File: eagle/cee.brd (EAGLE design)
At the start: 50 x 80 mm, 55 parts, among them IC1 IC1, J1 SOLDERJUMPERNC2

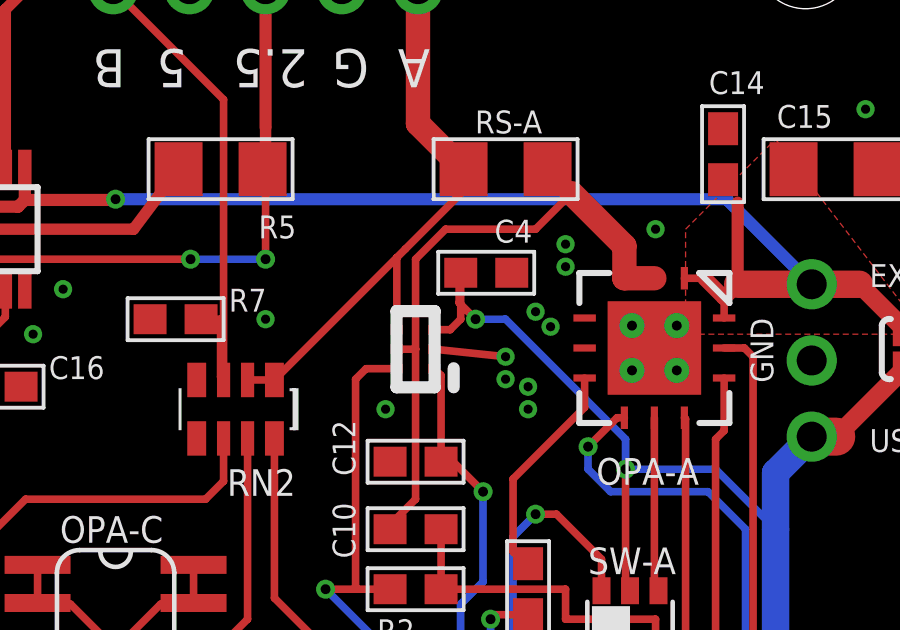
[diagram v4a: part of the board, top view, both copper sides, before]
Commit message: Update library (SC70 and QFN)
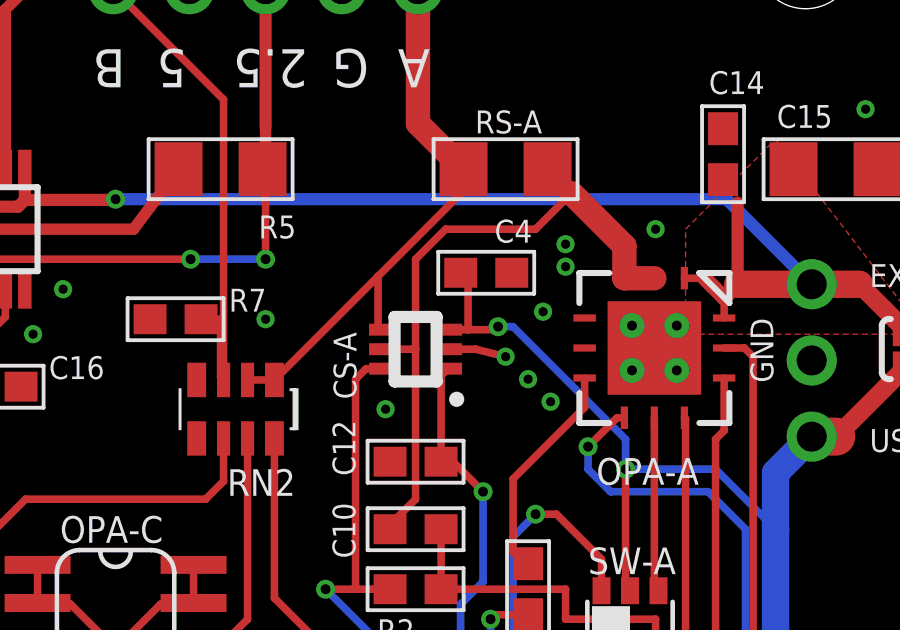
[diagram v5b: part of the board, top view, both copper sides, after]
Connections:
- net GND: now also OPA-A.P$2, OPA-A.P$4, OPA-A.P$6, OPA-A.P$7
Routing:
- net 5V: track 185.1 -> 183.6 mm
- net SMU-A: track 19.6 -> 19.0 mm
- net GND: track 22.6 -> 22.2 mm, vias 48 -> 46
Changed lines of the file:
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@@
 <wire x1="46.542" y1="59.6051" x2="44.0219" y2="57.085" width="0.6096" layer="1"/>
 <wire x1="44.0219" y1="57.085" x2="43.2052" y2="57.085" width="1.27" layer="1"/>
-<wire x1="30.625" y1="60.65" x2="31.155" y2="60.65" width="0.254" layer="1"/>
-<wire x1="31.155" y1="60.65" x2="31.505" y2="61" width="0.254" layer="1"/>
+<wire x1="31.1" y1="60.65" x2="31.155" y2="60.65" width="0.254" layer="1"/>
 <wire x1="42" y1="14" x2="42" y2="54" width="0.9144" layer="16"/>
 <wire x1="42" y1="54" x2="42" y2="55.8798" width="0.9144" layer="16"/>
@@
 <wire x1="13.85" y1="49.25" x2="14" y2="49.1" width="0.254" layer="1"/>
 <wire x1="14" y1="49.1" x2="14" y2="49" width="0.254" layer="1"/>
-<wire x1="31.505" y1="61" x2="31.505" y2="62.548" width="0.254" layer="1"/>
 <wire x1="31.505" y1="62.548" x2="31.452" y2="62.548" width="0.254" layer="1"/>
-<wire x1="31.452" y1="62.548" x2="31.452" y2="61.548" width="0.254" layer="1"/>
-<wire x1="31.452" y1="61.548" x2="32" y2="61" width="0.254" layer="1"/>
-<via x="32" y="61" extent="1-16" drill="0.3302"/>
-<wire x1="32" y1="61" x2="33" y2="61" width="0.254" layer="16"/>
-<wire x1="33" y1="61" x2="37" y2="57" width="0.254" layer="16"/>
+<via x="32.75" y="60.75" extent="1-16" drill="0.3302"/>
+<wire x1="32.75" y1="60.75" x2="33.25" y2="60.75" width="0.254" layer="16"/>
+<wire x1="33.25" y1="60.75" x2="37" y2="57" width="0.254" layer="16"/>
 <wire x1="37" y1="57" x2="37" y2="56" width="0.254" layer="16"/>
 <via x="37" y="56" extent="1-16" drill="0.3302"/>
@@
 <wire x1="37" y1="56" x2="40" y2="56" width="0.254" layer="16"/>
 <wire x1="40" y1="56" x2="42" y2="54" width="0.254" layer="16"/>
+<wire x1="32.75" y1="60.75" x2="32.65" y2="60.65" width="0.254" layer="1"/>
+<wire x1="32.65" y1="60.65" x2="31.75" y2="60.65" width="0.254" layer="1"/>
+<wire x1="31.75" y1="60.65" x2="31.1" y2="60.65" width="0.254" layer="1"/>
+<wire x1="31.505" y1="62.548" x2="31.75" y2="62.303" width="0.254" layer="1"/>
+<wire x1="31.75" y1="62.303" x2="31.75" y2="60.65" width="0.254" layer="1"/>
 </signal>
 <signal name="GND">
@@
 <via x="20" y="32" extent="1-16" drill="0.305"/>
 <via x="21.25" y="21.5" extent="1-16" drill="0.305"/>
-<via x="33.75" y="58" extent="1-16" drill="0.305"/>
 <via x="36" y="48" extent="1-16" drill="0.305"/>
 <via x="25" y="50" extent="1-16" drill="0.305"/>
@@
 <via x="35" y="62.75" extent="1-16" drill="0.305"/>
 <via x="33" y="59.75" extent="1-16" drill="0.305"/>
-<wire x1="30.625" y1="60" x2="33" y2="59.75" width="0.254" layer="1"/>
+<wire x1="31.1" y1="60" x2="32" y2="60" width="0.254" layer="1"/>
+<wire x1="32" y1="60" x2="33" y2="59.75" width="0.254" layer="1"/>
 <contactref element="C16" pad="2"/>
 <via x="30.5" y="30.25" extent="1-16" drill="0.3302" shape="octagon"/>
@@
 <contactref element="C17" pad="1"/>
 <via x="29" y="58" extent="1-16" drill="0.305"/>
-<via x="33" y="59" extent="1-16" drill="0.305"/>
-<via x="33.75" y="58.75" extent="1-16" drill="0.305"/>
+<via x="33.75" y="59" extent="1-16" drill="0.305"/>
+<via x="34.5" y="58.25" extent="1-16" drill="0.305"/>
 <via x="17" y="43.5" extent="1-16" drill="0.305"/>
 <via x="31.25" y="36.25" extent="1-16" drill="0.3302" shape="octagon"/>
@@
 <via x="34.25" y="38.25" extent="1-16" drill="0.3302" shape="octagon"/>
 <via x="27.75" y="45.25" extent="1-16" drill="0.3302" shape="octagon"/>
-<via x="34" y="61.25" extent="1-16" drill="0.305"/>
-<via x="34.5" y="60.75" extent="1-16" drill="0.305"/>
+<via x="34.25" y="61.25" extent="1-16" drill="0.305"/>
 <via x="5" y="43" extent="1-16" drill="0.305"/>
 <via x="17.25" y="60.5" extent="1-16" drill="0.305"/>
@@
 <via x="18.25" y="62" extent="1-16" drill="0.305"/>
 <wire x1="20" y1="30" x2="20.5" y2="29.5" width="0.254" layer="1"/>
+<contactref element="OPA-A" pad="P$2"/>
+<contactref element="OPA-A" pad="P$4"/>
+<contactref element="OPA-A" pad="P$6"/>
+<contactref element="OPA-A" pad="P$7"/>
 </signal>
 <signal name="PDI-DATA">
@@
 <wire x1="25.295" y1="58.975" x2="24.4" y2="58.975" width="0.254" layer="1"/>
 <wire x1="31.6" y1="66" x2="31.6" y2="65.28" width="0.254" layer="1"/>
-<wire x1="31.6" y1="65.28" x2="29.66" y2="63.34" width="0.254" layer="1"/>
-<wire x1="29.375" y1="63.055" x2="25.295" y2="58.975" width="0.254" layer="1"/>
-<wire x1="29.375" y1="60.65" x2="29.375" y2="63.055" width="0.254" layer="1"/>
-<wire x1="29.375" y1="63.055" x2="29.66" y2="63.34" width="0.254" layer="1"/>
+<wire x1="31.6" y1="65.28" x2="28.75" y2="62.43" width="0.254" layer="1"/>
+<wire x1="28.75" y1="62.43" x2="25.295" y2="58.975" width="0.254" layer="1"/>
+<wire x1="28.75" y1="62.43" x2="28.75" y2="60.75" width="0.254" layer="1"/>
+<wire x1="28.75" y1="60.75" x2="28.85" y2="60.65" width="0.254" layer="1"/>
+<wire x1="28.85" y1="60.65" x2="28.9" y2="60.65" width="0.254" layer="1"/>
 </signal>
 <signal name="EXP3">
@@
 <wire x1="36.96" y1="62.365" x2="37.96" y2="62.365" width="0.8128" layer="1"/>
 <wire x1="34" y1="64" x2="35.2" y2="65.2" width="0.254" layer="1"/>
-<wire x1="29.375" y1="60" x2="30" y2="60" width="0.254" layer="1"/>
+<wire x1="28.9" y1="60" x2="30" y2="60" width="0.254" layer="1"/>
 <wire x1="34" y1="64" x2="31" y2="64" width="0.254" layer="1"/>
 <wire x1="30" y1="60" x2="30" y2="63" width="0.254" layer="1"/>
@@
 <wire x1="32.6" y1="26.6" x2="33.25" y2="27.25" width="0.254" layer="1"/>
 <contactref element="CS-A" pad="P6"/>
-<wire x1="29.375" y1="59.35" x2="28.35" y2="59.35" width="0.254" layer="1"/>
+<wire x1="28.9" y1="59.35" x2="28.35" y2="59.35" width="0.254" layer="1"/>
 <wire x1="28.35" y1="59.35" x2="28" y2="59" width="0.254" layer="1"/>
 <wire x1="28" y1="59" x2="28" y2="52" width="0.254" layer="1"/>
@@
 <contactref element="C12" pad="1"/>
 <wire x1="30.85" y1="56.25" x2="30.85" y2="59.125" width="0.254" layer="1"/>
-<wire x1="30.85" y1="59.125" x2="30.625" y2="59.35" width="0.254" layer="1"/>
+<wire x1="30.85" y1="59.125" x2="31.1" y2="59.35" width="0.254" layer="1"/>
 <wire x1="30.85" y1="56.25" x2="31.25" y2="56.25" width="0.254" layer="1"/>
 <wire x1="31.25" y1="56.25" x2="32.25" y2="55.25" width="0.254" layer="1"/>

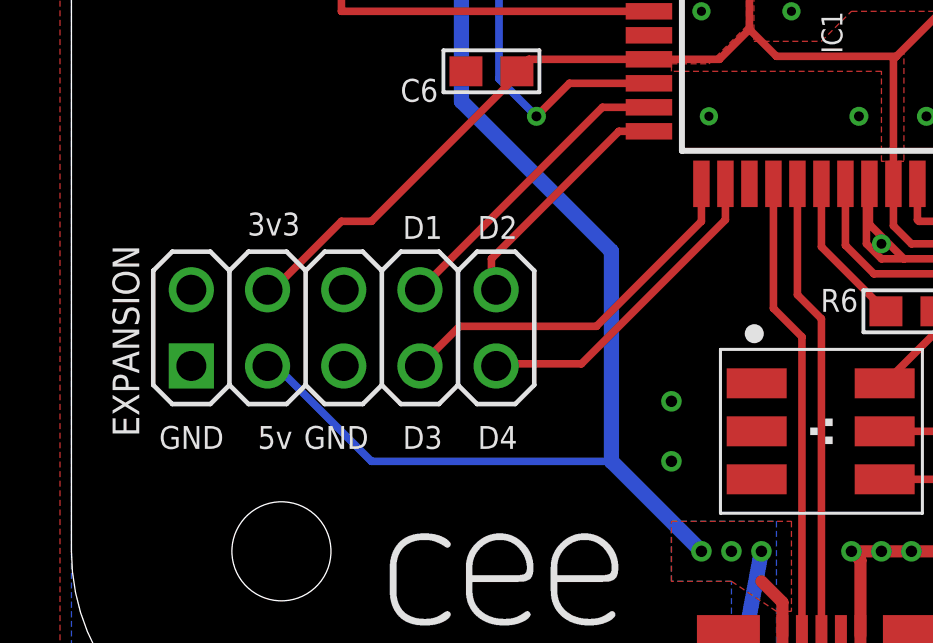
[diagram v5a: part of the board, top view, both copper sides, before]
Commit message: Break out another GPIO
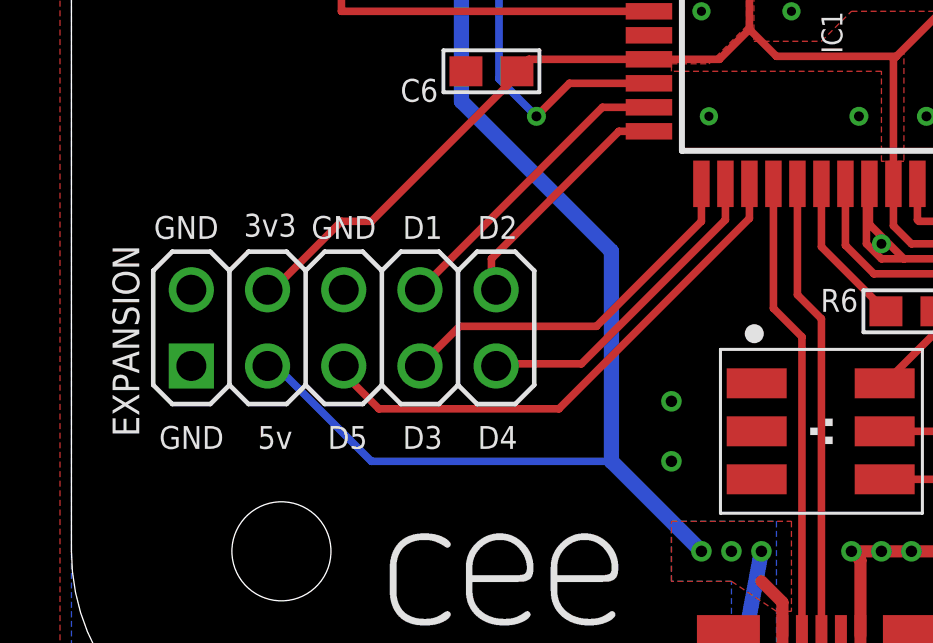
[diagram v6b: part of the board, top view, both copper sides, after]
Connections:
- new net EXP5: EXPANSION.5, IC1.25
- net GND: now also EXPANSION.2, EXPANSION.6; no longer EXPANSION.5
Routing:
- net EXP5: track 0.00 -> 18.1 mm
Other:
- board text added: "D5"
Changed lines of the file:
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@@
 <text x="47.7266" y="22.987" size="0.889" layer="25" ratio="12" rot="R90">3.3V</text>
 <text x="49.3014" y="16.2306" size="0.762" layer="25" font="vector" ratio="12" rot="R90">BOOT</text>
-<text x="7.62" y="18.288" size="0.762" layer="25" font="vector" ratio="11" rot="R180">3v3</text>
+<text x="7.5" y="18.25" size="0.762" layer="25" font="vector" ratio="11" rot="R180">3v3</text>
 <text x="5.08" y="11.176" size="0.762" layer="25" font="vector" ratio="11" rot="R180">GND</text>
 <text x="7.366" y="11.176" size="0.762" layer="25" font="vector" ratio="11" rot="R180">5v</text>
@@
 <text x="26.4" y="70" size="1.27" layer="25" font="vector" ratio="12" rot="SR180">2.5</text>
 <text x="28.44" y="70" size="1.27" layer="25" font="vector" ratio="12" rot="SR180">G</text>
-<text x="9.906" y="11.176" size="0.762" layer="25" font="vector" ratio="11" rot="R180">GND</text>
+<text x="10.156" y="18.176" size="0.762" layer="25" font="vector" ratio="11" rot="R180">GND</text>
 <text x="12.366" y="18.176" size="0.762" layer="25" font="vector" ratio="11" rot="R180">D1</text>
 <text x="14.866" y="18.176" size="0.762" layer="25" font="vector" ratio="11" rot="R180">D2</text>
@@
 <text x="41.926" y="58.884" size="0.762" layer="25" font="vector" ratio="11" rot="R90">GND</text>
 <text x="48.676" y="58.884" size="0.762" layer="25" font="vector" ratio="11" rot="R90">SJ1</text>
+<text x="4.906" y="18.176" size="0.762" layer="25" font="vector" ratio="11" rot="R180">GND</text>
+<text x="9.866" y="11.176" size="0.762" layer="25" font="vector" ratio="11" rot="R180">D5</text>
 </plain>
 <attributes>
@@
 <contactref element="JP1" pad="2"/>
 <contactref element="JP5" pad="2"/>
-<contactref element="EXPANSION" pad="5"/>
 <polygon width="0.4064" layer="16" isolate="0.3048" rank="3">
 <vertex x="0" y="80"/>
@@
 <contactref element="OPA-A" pad="P$6"/>
 <contactref element="OPA-A" pad="P$7"/>
+<contactref element="EXPANSION" pad="2"/>
+<contactref element="EXPANSION" pad="6"/>
 </signal>
 <signal name="PDI-DATA">
@@
 <wire x1="19.2" y1="25.75" x2="19.25" y2="25.8" width="0.254" layer="1"/>
 </signal>
+<signal name="EXP5">
+<contactref element="IC1" pad="25"/>
+<contactref element="EXPANSION" pad="5"/>
+<wire x1="22.6" y1="19.25" x2="22.6" y2="18.1" width="0.254" layer="1"/>
+<wire x1="22.6" y1="18.1" x2="16.25" y2="11.75" width="0.254" layer="1"/>
+<wire x1="16.25" y1="11.75" x2="10.25" y2="11.75" width="0.254" layer="1"/>
+<wire x1="10.25" y1="11.75" x2="9" y2="13" width="0.254" layer="1"/>
+<wire x1="9.077" y1="13.178" x2="9.077" y2="13.077" width="0.254" layer="1"/>
+<wire x1="9.077" y1="13.077" x2="9" y2="13" width="0.254" layer="1"/>
+</signal>
 </signals>

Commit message: Update OPA567
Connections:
- net GND: now also OPA-A.P$1
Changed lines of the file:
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@@
 <contactref element="EXPANSION" pad="2"/>
 <contactref element="EXPANSION" pad="6"/>
+<contactref element="OPA-A" pad="P$1"/>
 </signal>
 <signal name="PDI-DATA">
@@
 </signal>
 </signals>
-<errors>
-</errors>
 </board>
 </drawing>

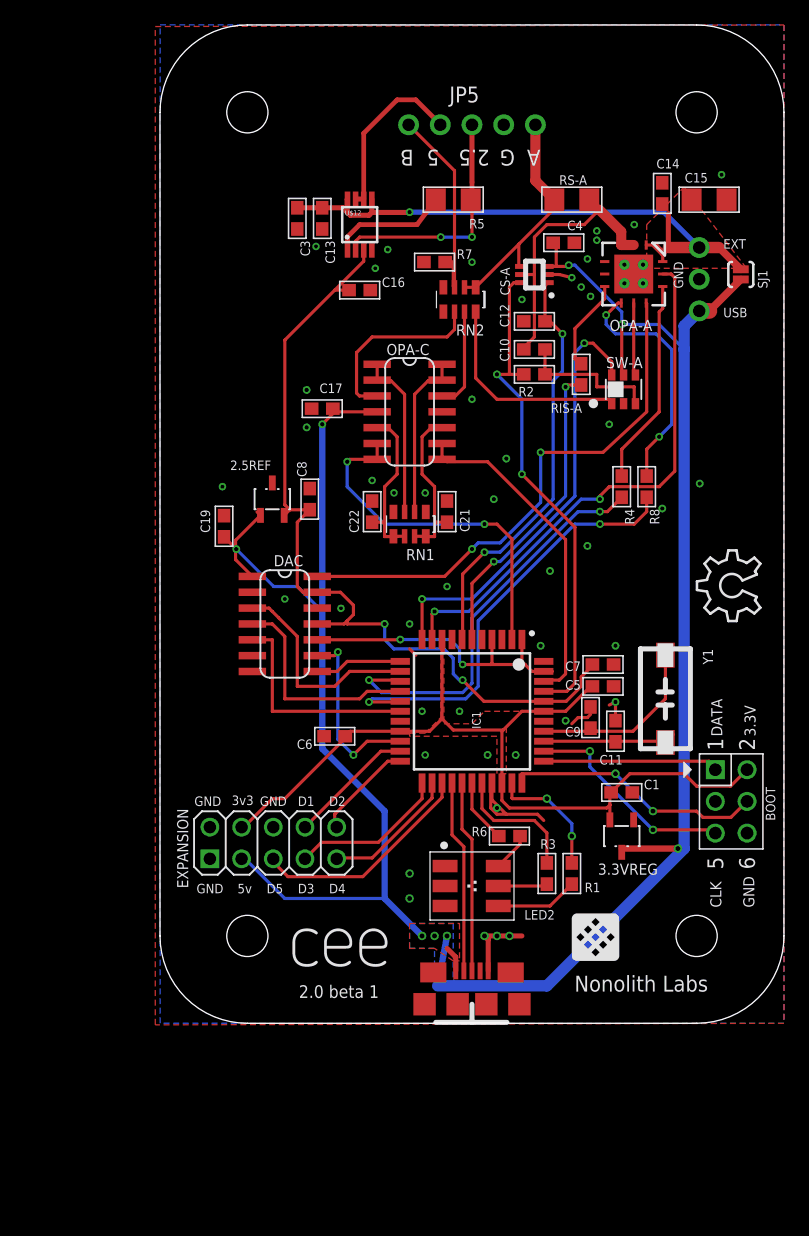
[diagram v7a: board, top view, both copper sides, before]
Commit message: significantly revised schematic including feedback compensation loooooops and mcp6n11
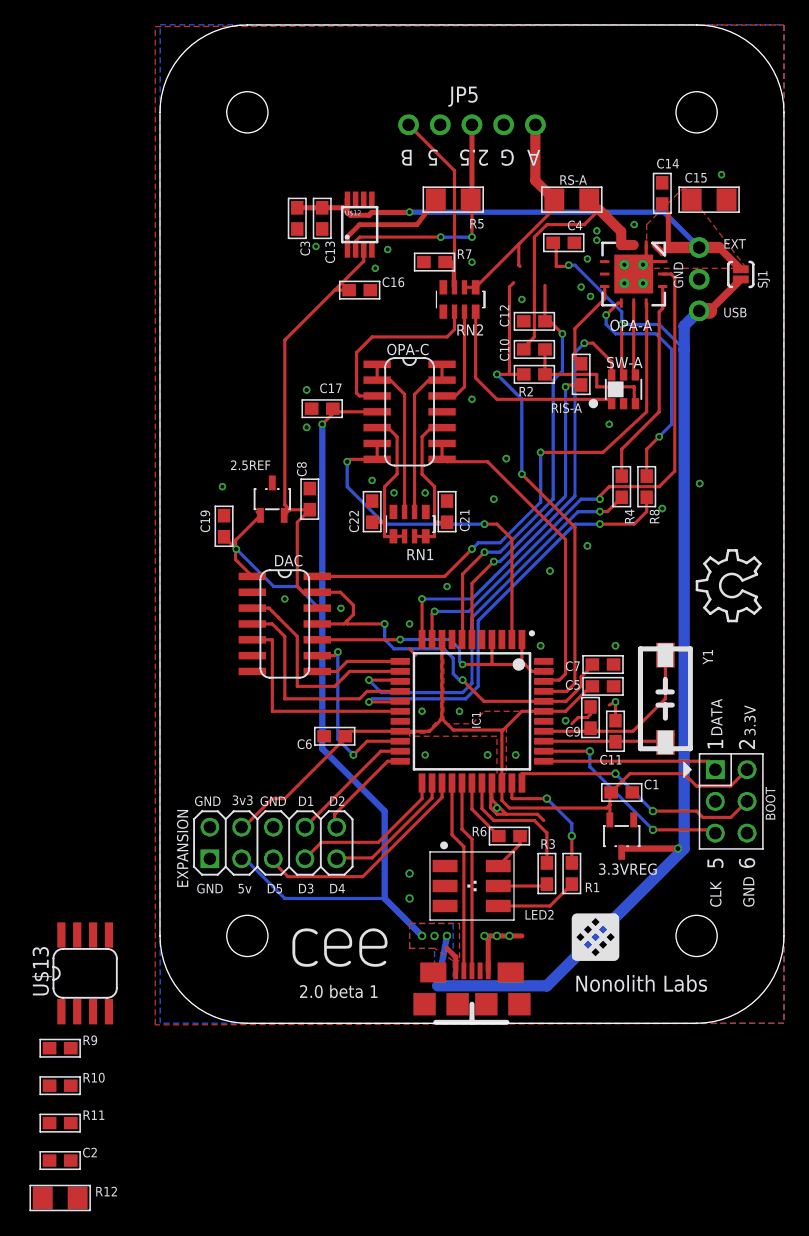
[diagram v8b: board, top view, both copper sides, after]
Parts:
- removed CS-A: INA213, nonolith:SC-70
- added C2, R11: (no value), nonolith:0603
- added R10: 100k, nonolith:0603
- added R12: 15o, nonolith:1206
- added R9: 1k, nonolith:0603
- added U$13: MCP6N11, nonolith:SO-08
- R5: value 15o -> 5o
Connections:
- removed net 5VOUT: JP5.4, U$12.6, U$12.7
- new net AF-2.5: C2.2, R11.1
- new net EN-CSA: U$13.8
- new net N$14: JP5.4, R12.2
- new net VFG: R10.2, R9.1, U$13.1
- net 2.5VFDBK: now also R11.2
- net 2.5VOUT: now also C2.1
- net 5V: now also U$13.7; no longer CS-A.P3
- net 5V-EXT: now also R12.1; no longer OPA-A.1, OPA-A.12, U$12.5
- net CSA-VREF: now also R9.2, U$13.5; no longer CS-A.P1
- net GND: now also OPA-A.1, OPA-A.12, OPA-A.GNDPAD, OPA-A.GNDPAD1, OPA-A.GNDPAD2, OPA-A.GNDPAD3, OPA-A.GNDPAD4, U$13.4; no longer CS-A.P2, OPA-A.P$1, OPA-A.P$2, OPA-A.P$4, OPA-A.P$6, OPA-A.P$7
- net SMU-A: now also U$13.2; no longer CS-A.P4
- net VO-A: now also U$13.3; no longer CS-A.P5
- net VS-A: now also R10.1, U$13.6; no longer CS-A.P6
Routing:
- net 5VOUT: track 14.1 -> 0.00 mm
- net 5V-EXT: track 48.0 -> 45.6 mm
- net GND: track 22.2 -> 23.8 mm, vias 46 -> 45
- net VO-A: track 22.3 -> 21.2 mm
- net 5V: track 183.6 -> 182.9 mm
- net VS-A: track 40.3 -> 39.8 mm
